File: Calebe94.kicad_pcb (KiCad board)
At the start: 2 copper layers, 248.9 x 96.4 mm, 107 parts, among them J1 USB_B, SW1 SW_DIP_x01, SW10 SW_DIP_x01, SW11 SW_DIP_x01, SW12 SW_DIP_x01, SW13 SW_DIP_x01, SW14 SW_DIP_x01, SW15 SW_DIP_x01, SW16 SW_DIP_x01, SW17 SW_DIP_x01, SW18 SW_DIP_x01, SW19 SW_DIP_x01, SW2 SW_DIP_x01, SW20 SW_DIP_x01, SW21 SW_DIP_x01, SW22 SW_DIP_x01, SW23 SW_DIP_x01, SW24 SW_DIP_x01, SW25 SW_DIP_x01, SW26 SW_DIP_x01, SW27 SW_DIP_x01, SW28 SW_DIP_x01, SW29 SW_DIP_x01, SW3 SW_DIP_x01, SW30 SW_DIP_x01, SW31 SW_DIP_x01, SW32 SW_DIP_x01, SW33 SW_DIP_x01, SW34 SW_DIP_x01, SW35 SW_DIP_x01, SW36 SW_DIP_x01, SW37 SW_DIP_x01, SW38 SW_DIP_x01, SW39 SW_DIP_x01, SW4 SW_DIP_x01, SW40 SW_DIP_x01, SW41 SW_DIP_x01, SW42 SW_DIP_x01, SW43 SW_DIP_x01, SW44 SW_DIP_x01, SW45 SW_DIP_x01, SW46 SW_DIP_x01, SW47 SW_DIP_x01, SW48 SW_DIP_x01, SW49 RESET, SW5 SW_DIP_x01, SW50 BOOT, SW6 SW_DIP_x01, SW7 SW_DIP_x01, SW8 SW_DIP_x01, SW9 SW_DIP_x01, U1 ARDUINO_PRO_MINI

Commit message: Changed routes
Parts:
- SW1: footprint keyboard_parts:ALPS_SKCM_reverse_pad -> keyboard_parts:ALPS_SKCM
- turned SW1 to 180 degrees
- turned SW11 to 180 degrees
- turned SW13 to 180 degrees
- turned SW15 to 180 degrees
- turned SW17 to 180 degrees
- turned SW19 to 180 degrees
- turned SW21 to 180 degrees
- turned SW23 to 180 degrees
- turned SW25 to 180 degrees
- turned SW27 to 180 degrees
- turned SW29 to 180 degrees
- turned SW3 to 180 degrees
- turned SW31 to 180 degrees
- turned SW33 to 180 degrees
- turned SW35 to 180 degrees
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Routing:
- net ROW_0: track 0.00 -> 268.2 mm
- net ROW_3: track 0.00 -> 247.9 mm
- net ROW_1: track 0.00 -> 247.9 mm
- net ROW_2: track 0.00 -> 232.2 mm
- net COL_0: track 0.00 -> 150.6 mm
- net COL_11: track 0.00 -> 148.3 mm
- net GND: track 0.00 -> 142.3 mm
- net +5V: track 0.00 -> 132.9 mm
- net COL_9: track 0.00 -> 130.9 mm
- net COL_1: track 0.00 -> 128.2 mm
- net COL_10: track 0.00 -> 128.0 mm, vias 0 -> 1
- net COL_2: track 0.00 -> 109.9 mm
- net COL_8: track 0.00 -> 109.2 mm, vias 0 -> 1
- net COL_3: track 0.00 -> 94.6 mm
- net COL_7: track 0.00 -> 87.2 mm
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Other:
- board size 248.9 x 96.4 mm -> 248.8 x 96.4 mm

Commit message: Added appa and my logo as silk
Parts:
- added Calebe94: Calebe94, ARDUINO_PRO_MINI:calebe94, F.Cu at (49.4, 122.8)
- added G***: LOGO, ARDUINO_PRO_MINI:appa, F.Cu at (154.1, 95.2)
- added J2: USB, Connector_PinSocket_2.54mm:PinSocket_1x05_P2.54mm_Vertical, F.Cu at (167.8, 57.4)
- added J3: Columns, Connector_PinSocket_2.54mm:PinSocket_1x12_P2.54mm_Vertical, F.Cu at (63.5, 93.5)
- added J4: Rows, Connector_PinSocket_2.54mm:PinSocket_1x04_P2.54mm_Vertical, F.Cu at (58.7, 87.2)
- added J5: I2C, Connector_PinSocket_2.54mm:PinSocket_1x04_P2.54mm_Vertical, F.Cu at (205.9, 57.2)
- moved U1 95.6 mm to (249.9, 94.0)
- moved D49 24.9 mm to (154.0, 93.2), turned to 90 degrees
- moved R1 5.59 mm to (148.2, 93.5)
- moved J1 5.37 mm to (152.8, 65.8)
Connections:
- U1 pad JP7_10: unconnected-(U1-PadJP7_10) -> RESET
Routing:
- net COL_5: track 59.0 -> 232.7 mm
- net COL_4: track 63.6 -> 229.7 mm
- net COL_6: track 72.6 -> 226.6 mm, vias 1 -> 0
- net COL_7: track 87.2 -> 239.1 mm
- net GND: track 142.3 -> 0.00 mm
- net COL_3: track 94.6 -> 234.4 mm
- net COL_8: track 109.2 -> 242.3 mm, vias 1 -> 0
- net COL_2: track 109.9 -> 232.5 mm
- net D-: track 6.58 -> 127.4 mm, vias 0 -> 1
- net COL_1: track 128.2 -> 247.0 mm
- net COL_9: track 130.9 -> 240.0 mm
- net COL_10: track 128.0 -> 233.0 mm, vias 1 -> 0
- net D+: track 20.0 -> 118.2 mm
- net +5V: track 132.9 -> 222.4 mm
- net COL_0: track 150.6 -> 239.9 mm
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- added copper zone on B.Cu, net GND
- added copper zone on F.Cu, net GND
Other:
- board size 248.8 x 96.4 mm -> 228.4 x 76.1 mm
- board text added: "5V"
- board text added: "A0"
- board text added: "A1"
- board text added: "A2"
- board text added: "A3"
- board text added: "A4"
- board text added: "A5"
- board text added: "COL0"
- board text added: "COL1"
- board text added: "COL10"
- board text added: "COL11"
- board text added: "COL2"
- board text added: "COL3"
- board text added: "COL4"
- board text added: "COL5"
- board text added: "COL6"
- board text added: "COL7"
- board text added: "COL8"
- board text added: "COL9"
- board text added: "D+"
- board text added: "D-"
- board text added: "D10"
- board text added: "D11"
- board text added: "D12"
- board text added: "D13"
- board text added: "D2"
- board text added: "D3"
- board text added: "D4"
- board text added: "D5"
- board text added: "D6"
- board text added: "D7"
- board text added: "D8"
- board text added: "D9"
- board text added: "DTR"
- board text added: "GND"
- board text added: "RAW"
- board text added: "ROW0"
- board text added: "ROW1"
- board text added: "ROW2"
- board text added: "ROW3"
- board text added: "RST"
- board text added: "RXD"
- board text added: "SCL"
- board text added: "SDA"
- board text added: "TXD"

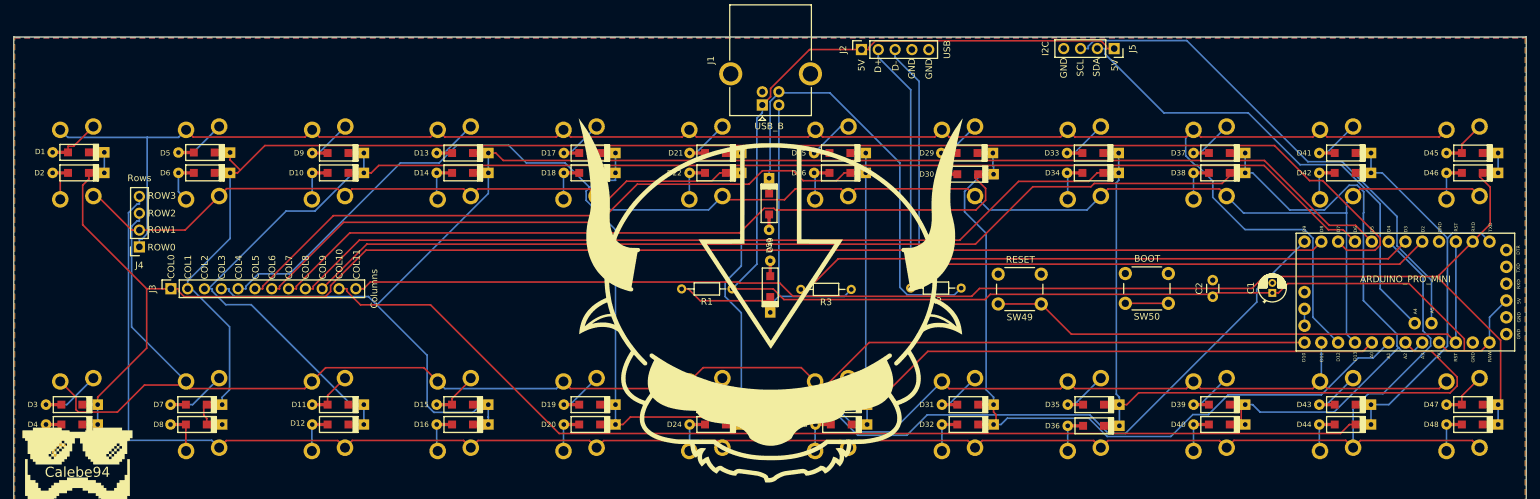
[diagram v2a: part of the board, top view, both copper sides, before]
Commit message: Changed switches layout to be read from left to right
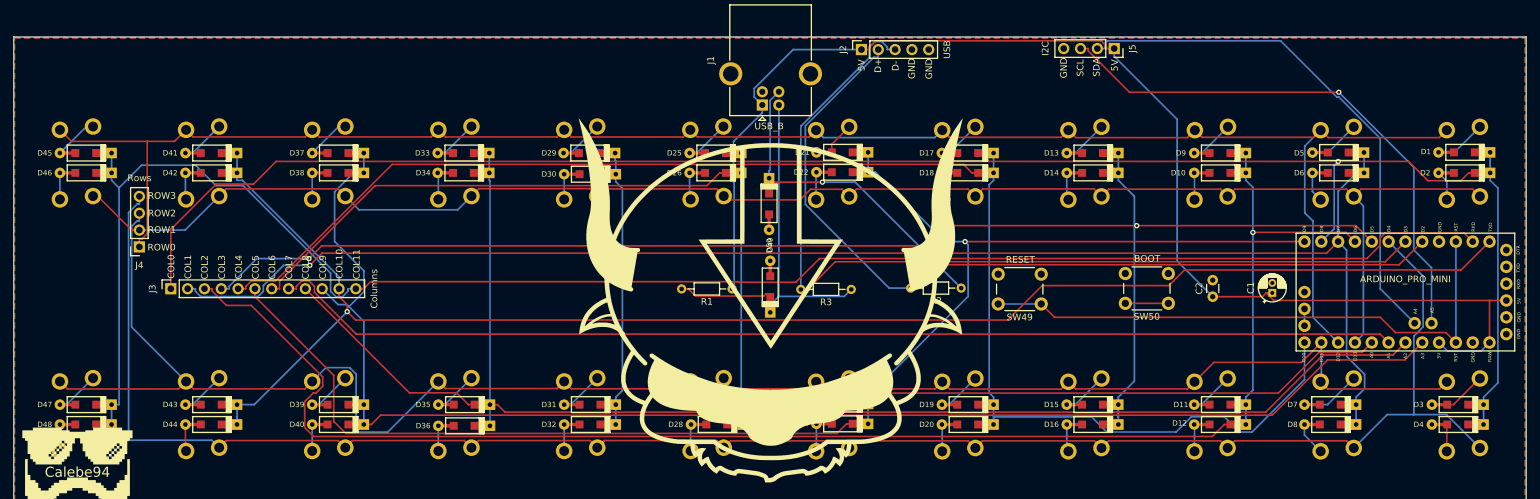
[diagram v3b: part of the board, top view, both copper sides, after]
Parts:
- moved SW1 209.4 mm to (258.6, 65.0)
- moved SW2 209.4 mm to (258.6, 84.0)
- moved SW3 209.4 mm to (258.6, 103.0)
- moved SW4 209.4 mm to (258.6, 122.0)
- moved SW45 209.4 mm to (49.2, 65.0)
- moved SW46 209.4 mm to (49.2, 84.0)
- moved SW47 209.4 mm to (49.2, 103.0)
- moved SW48 209.4 mm to (49.2, 122.0)
- moved D45 209.4 mm to (50.6, 73.0)
- moved D46 209.4 mm to (50.6, 76.0)
- moved D47 209.4 mm to (50.6, 111.0)
- moved D48 209.4 mm to (50.6, 114.0)
- moved D1 209.3 mm to (258.8, 72.9)
- moved D2 209.3 mm to (258.8, 76.0)
- moved D3 209.3 mm to (257.8, 111.0)
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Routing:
- net COL_11: track 225.0 -> 273.1 mm
- net COL_0: track 239.9 -> 276.8 mm, vias 0 -> 1
- net +5V: track 222.4 -> 195.7 mm
- net COL_7: track 239.1 -> 222.4 mm, vias 0 -> 1
- net Net-(D50-Pad1): track 67.6 -> 51.6 mm, vias 0 -> 1
- net COL_8: track 242.3 -> 226.4 mm
- net COL_1: track 247.0 -> 233.2 mm, vias 0 -> 1
- net COL_9: track 240.0 -> 226.9 mm
- net D-: track 127.4 -> 140.1 mm, vias 1 -> 0
- net ROW_0: track 284.0 -> 271.7 mm
- net COL_5: track 232.7 -> 221.2 mm, vias 0 -> 1
- net D+: track 118.2 -> 129.6 mm
- net COL_10: track 233.0 -> 244.0 mm, vias 0 -> 1
- net COL_2: track 232.5 -> 240.9 mm, vias 0 -> 1
- net ROW_3: track 297.0 -> 289.1 mm
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
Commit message: Added gerber folder
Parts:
- added C3: 22p, Capacitor_THT:C_Disc_D3.0mm_W1.6mm_P2.50mm, F.Cu at (128.8, 103.2)
- added C4: 22p, Capacitor_THT:C_Disc_D3.0mm_W1.6mm_P2.50mm, F.Cu at (114.1, 103.2)
- added C5: C, Capacitor_THT:C_Disc_D4.3mm_W1.9mm_P5.00mm, F.Cu at (118.1, 86.2)
- added G1: LOGO, ARDUINO_PRO_MINI:gpl3, F.Cu at (258.2, 124.5)
- added J6: ICSP, Connector_PinSocket_2.54mm:PinSocket_2x03_P2.54mm_Vertical, F.Cu at (44.2, 92.2)
- added R4: 10k, Resistor_THT:R_Axial_DIN0204_L3.6mm_D1.6mm_P7.62mm_Horizontal, F.Cu at (175.3, 91.9)
- added U2: ATmega328-P, Package_DIP:DIP-28_W7.62mm, F.Cu at (99.0, 97.8)
- added Y1: 16MHz, Crystal:Crystal_HC18-U_Vertical, F.Cu at (123.7, 103.2)
- C1: value C_Polarized -> C
- moved R1 34.7 mm to (182.8, 95.3)
- moved R2 16.6 mm to (166.3, 92.2)
- moved SW49 9.40 mm to (204.3, 95.7)
- moved C1 5.85 mm to (223.9, 94.2)
- moved C2 2.45 mm to (218.3, 94.8)
- moved R3 1.70 mm to (166.3, 95.3)
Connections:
- net +5V renamed VCC
- net ROW_0 renamed MISO
- net ROW_2 renamed MOSI
- U1 pad JP1_1: unconnected-(U1-PadJP1_1) -> RESET
- U1 pad JP1_2: unconnected-(U1-PadJP1_2) -> TXD
- U1 pad JP1_3: unconnected-(U1-PadJP1_3) -> RXD
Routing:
- net GND: track 0.00 -> 366.7 mm
- net RXD: track 0.00 -> 171.5 mm
- net VCC: track 195.7 -> 365.1 mm
- net TXD: track 0.00 -> 166.0 mm
- net RESET: track 86.8 -> 247.0 mm
- net SCL: track 82.6 -> 217.4 mm, vias 1 -> 2
- net SDA: track 79.8 -> 199.3 mm, vias 0 -> 2
- net D+: track 129.6 -> 192.6 mm, vias 0 -> 1
- net COL_1: track 233.2 -> 289.8 mm, vias 1 -> 0
- net MISO: track 271.7 -> 324.7 mm
- net D-: track 140.1 -> 188.7 mm, vias 0 -> 1
- net ROW_1: track 247.3 -> 282.3 mm
- net COL_0: track 276.8 -> 310.9 mm
- net COL_6: track 225.8 -> 246.5 mm
- net COL_4: track 229.8 -> 250.4 mm
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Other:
- board size 228.4 x 76.1 mm -> 227.8 x 75.4 mm
- board text added: "27/10/2022"
- board text added: "APPA Keyboard"
- board text added: "MISO"
- board text added: "MOSI"
- board text added: "RESET"
- board text added: "SCK"
- board text added: "VCC"
- board text added: "calebe.dev.br"
